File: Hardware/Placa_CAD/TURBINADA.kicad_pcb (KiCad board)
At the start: 4 copper layers, 110 x 102 mm, 49 parts, among them J1 TURBINA, J2 RESISTENCIAS, J3 BATERIA, J4 ICSP, Q1 IXTP44P15T, Q2 IXTP36P15P, Q3 FQN1N50C, Q4 FQN1N50C, U1 PIC16F18324-xSL, U2 ADP2302ARDZ-5.0

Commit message: Finished board layout
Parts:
- L2: footprint footprints:IHXL1500VZEB1R5M51 -> footprints:IHXL1500VZEB2R2M51
- R1: value 10K -> 52.3K
- R2: value 5K -> 10K
- moved L2 26.7 mm to (174.1, 115.4), turned to 90 degrees
- moved J1 2.00 mm to (156.8, 65.5)
- moved J3 1.25 mm to (192.6, 135.5)
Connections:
- L2 pad 1: Net-(D6-K) -> Net-(C10-Pad1)
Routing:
- net Net-(Q4-G): track 0.00 -> 52.0 mm
- net +5V: track 42.7 -> 0.00 mm
- net OUT_VOLTAGE: track 3.80 -> 43.7 mm
- net BAT_VOLTAGE: track 0.00 -> 36.0 mm
- net Net-(U1-RC5): track 0.00 -> 31.8 mm
- net Net-(Q3-G): track 0.00 -> 29.9 mm
- net Net-(U1-RC4): track 0.00 -> 28.1 mm
- net Net-(U1-RA2): track 2.44 -> 29.6 mm
- net Net-(U1-RC3): track 0.00 -> 24.7 mm
- net Net-(J4-Pin_1): track 0.00 -> 19.3 mm
- net Net-(J4-Pin_5): track 0.00 -> 18.2 mm
- net Net-(D2-K): track 18.1 -> 0.00 mm
- net Net-(J4-Pin_4): track 0.00 -> 15.9 mm
- net GND: track 0.00 -> 13.6 mm, vias 0 -> 6
- net Net-(U2-FB): track 0.00 -> 13.3 mm
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- added copper zone on B.Cu, net +5V
- added copper zone on F.Cu, net +5V
- added copper zone on In1.Cu, net +5V
- added copper zone on In4.Cu, net +5V
- added copper zone on In1.Cu, net /VCC Turbina (0 ~ 115V)
- added copper zone on In4.Cu, net /VCC Turbina (0 ~ 115V)
- added copper zone on In2.Cu, net GND
- added copper zone on In3.Cu, net GND
- added copper zone on In1.Cu, net Net-(C10-Pad1)
- added copper zone on In4.Cu, net Net-(C10-Pad1)
- added copper zone on F.Cu, net Net-(D2-K)
- added copper zone on In1.Cu, net Net-(D6-K)
- added copper zone on In4.Cu, net Net-(D6-K)
- added copper zone on In1.Cu, net Net-(D7-K)
- added copper zone on In4.Cu, net Net-(D7-K)
- added copper zone on B.Cu, net Net-(J1-Pin_1)
- added copper zone on F.Cu, net Net-(J1-Pin_1)
- added copper zone on In1.Cu, net Net-(J1-Pin_1)
- added copper zone on In4.Cu, net Net-(J1-Pin_1)
- added copper zone on B.Cu, net Net-(J1-Pin_2)
- added copper zone on F.Cu, net Net-(J1-Pin_2)
- added copper zone on In1.Cu, net Net-(J1-Pin_2)
- added copper zone on In4.Cu, net Net-(J1-Pin_2)
- added copper zone on B.Cu, net Net-(J1-Pin_3)
- added copper zone on F.Cu, net Net-(J1-Pin_3)
- added copper zone on In1.Cu, net Net-(J1-Pin_3)
- added copper zone on In4.Cu, net Net-(J1-Pin_3)
- added copper zone on In1.Cu, net Net-(J2-Pin_1)
- added copper zone on In4.Cu, net Net-(J2-Pin_1)
- removed copper zone on In1.Cu, net GND
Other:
- board size 110 x 102 mm -> 106.5 x 105.5 mm
- copper layers 4 -> 6

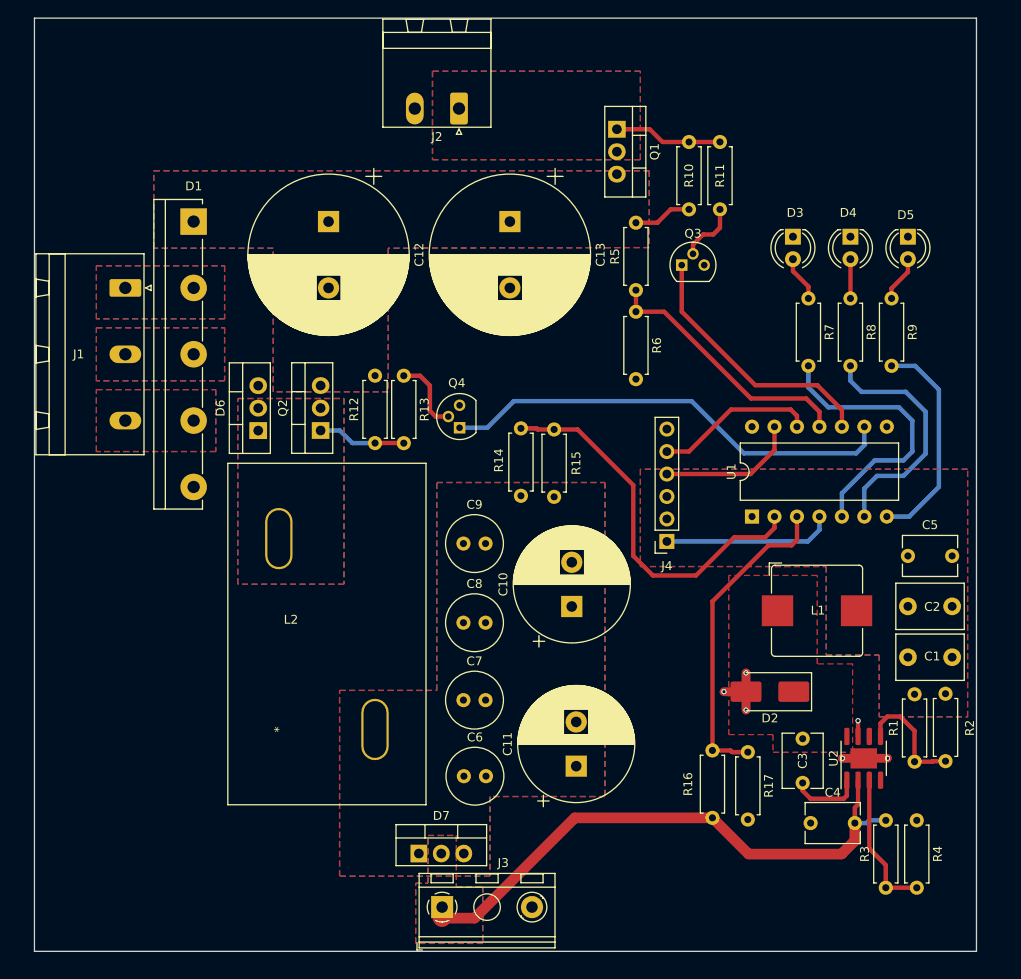
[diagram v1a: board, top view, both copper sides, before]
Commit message: Fixed a BAT connector track in the layout
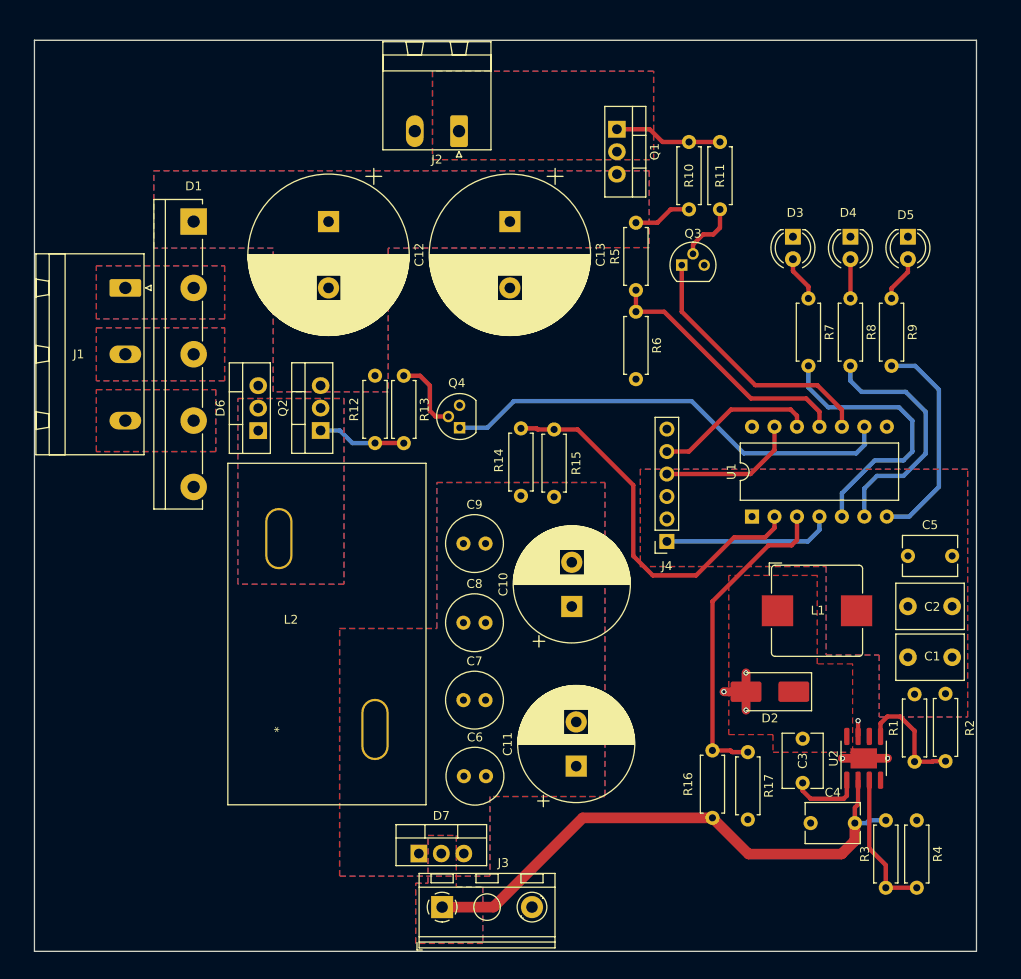
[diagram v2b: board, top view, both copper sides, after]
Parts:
- moved J2 2.56 mm to (194.5, 47.8)
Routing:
- net Net-(D7-K): track 64.4 -> 63.8 mm
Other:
- board size 106.5 x 105.5 mm -> 106.5 x 103 mm
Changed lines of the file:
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@@
   )
   (footprint "Connector_Phoenix_MSTB:PhoenixContact_MSTBA_2,5_2-G_1x02_P5.00mm_Horizontal" (layer "F.Cu")
-    (at 194.5 45.2225 180)
+    (at 194.5 47.7775 180)
     (descr "Generic Phoenix Contact connector footprint for: MSTBA_2,5/2-G; number of pins: 02; pin pitch: 5.00mm; Angled || order number: 1757475 12A || order number: 1923759 16A (HC)")
     (tags "phoenix_contact connector MSTBA_01x02_G_5.00mm")
@@
     )
   )
-  (gr_rect (start 146.5 35) (end 253 140.5)
+  (gr_rect (start 146.5 37.5) (end 253 140.5)
     (stroke (width 0.1) (type default)) (fill none) (layer "Edge.Cuts"))
   (dimension (type aligned) (layer "F.Fab")
-    (pts (xy 253 35) (xy 253 140.5))
+    (pts (xy 253 37.5) (xy 253 140.5))
     (height -4)
-    (gr_text "105.5000 mm" (at 255.85 87.75 90) (layer "F.Fab")
+    (gr_text "103.0000 mm" (at 255.85 89 90) (layer "F.Fab")
       (effects (font (size 1 1) (thickness 0.15)))
     )
@@
   (segment (start 233.35 122.35) (end 233.35 121.46) (width 0.5) (layer "F.Cu") (net 3))
   (segment (start 238.345 122.905) (end 238 123.25) (width 0.5) (layer "F.Cu") (net 3))
-  (segment (start 223.15 125.41) (end 207.59 125.41) (width 1.2) (layer "F.Cu") (net 4))
-  (segment (start 192.5 136.66) (end 192.59 136.75) (width 2) (layer "F.Cu") (net 4))
+  (segment (start 198.4 135.5) (end 192.59 135.5) (width 1.2) (layer "F.Cu") (net 4))
+  (segment (start 223.15 125.41) (end 208.49 125.41) (width 1.2) (layer "F.Cu") (net 4))
+  (segment (start 208.49 125.41) (end 198.4 135.5) (width 1.2) (layer "F.Cu") (net 4))
   (segment (start 239.25 126) (end 239.25 128) (width 1.2) (layer "F.Cu") (net 4))
-  (segment (start 207.59 125.41) (end 196.25 136.75) (width 1.2) (layer "F.Cu") (net 4))
   (segment (start 239.25 124.25) (end 239.25 126) (width 0.5) (layer "F.Cu") (net 4))
   (segment (start 227.24 129.5) (end 223.15 125.41) (width 1.2) (layer "F.Cu") (net 4))
@@
   (segment (start 239.25 128) (end 237.75 129.5) (width 1.2) (layer "F.Cu") (net 4))
   (segment (start 239.615 121.155) (end 239.615 123.885) (width 0.5) (layer "F.Cu") (net 4))
-  (segment (start 196.25 136.75) (end 192.59 136.75) (width 1.2) (layer "F.Cu") (net 4))
   (segment (start 240.55 126) (end 239.25 126) (width 0.5) (layer "B.Cu") (net 4))
   (segment (start 242.75 125.69) (end 240.86 125.69) (width 0.5) (layer "B.Cu") (net 4))
@@
     (connect_pads (clearance 1))
     (min_thickness 0.2) (filled_areas_thickness no)
-    (fill yes (thermal_gap 0.2) (thermal_bridge_width 1))
+    (fill yes (thermal_gap 0.2) (thermal_bridge_width 1.2))
     (polygon
       (pts
@@
         (xy 191.5 41)
         (xy 191.5 51)
-        (xy 215 51)
-        (xy 215 41)
+        (xy 216.5 51)
+        (xy 216.5 41)
       )
     )
@@
       (pts
         (xy 181 132)
-        (xy 181 111)
-        (xy 192 111)
+        (xy 181 104)
+        (xy 192 104)
         (xy 192 87.5)
         (xy 211 87.5)
